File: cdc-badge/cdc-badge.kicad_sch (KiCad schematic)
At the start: 137 parts, among them J1 USB_C, J2 JST S2B-PH-SM4-TB, J3 Conn_02x20_Odd_Even, J4 Conn_Grove, J5 Conn_02x03_Odd_Even, J6 Conn_01x06, J7 Conn_01x24, Q1 Si1308EDL, Q2 SS8050, SW0 0, SW1 1, SW10 YES, SW11 NO, SW12 power on/reset, SW13 reset, SW14 flash/power off, SW15 MST-22D18G2 3J, SW16 MST-22D18G2 3J, SW2 2, SW3 3, SW4 4, SW5 5, SW6 6, SW7 7, SW8 8, SW9 9, U1 ESP32-S3-WROOM-1-N16R8, U2 TCA9535PWR, U3 TROPIC01, U4 TPS613222ADBV, U6 BQ25895RTW, U7 USBLC6-2SC6, U8 TLV62569DBV

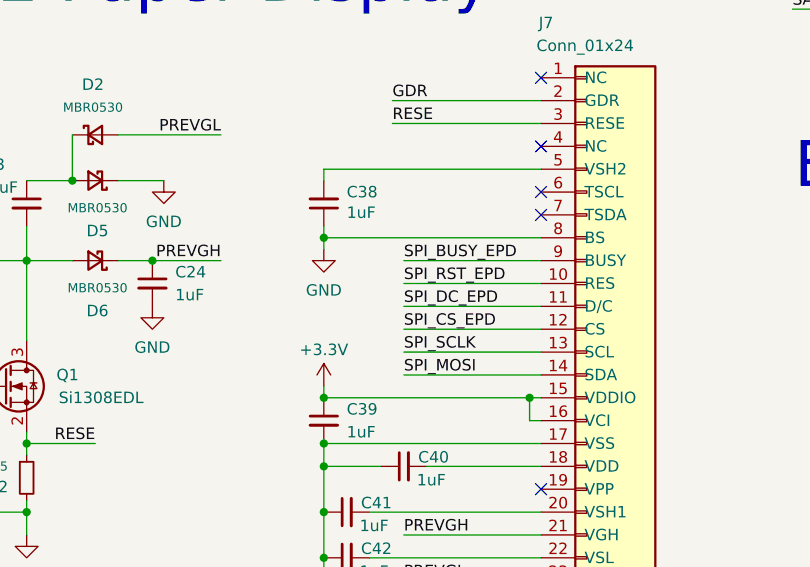
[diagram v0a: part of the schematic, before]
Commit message: schematic: ceetee reviews, e-paper display
Add pull-up on chip select.
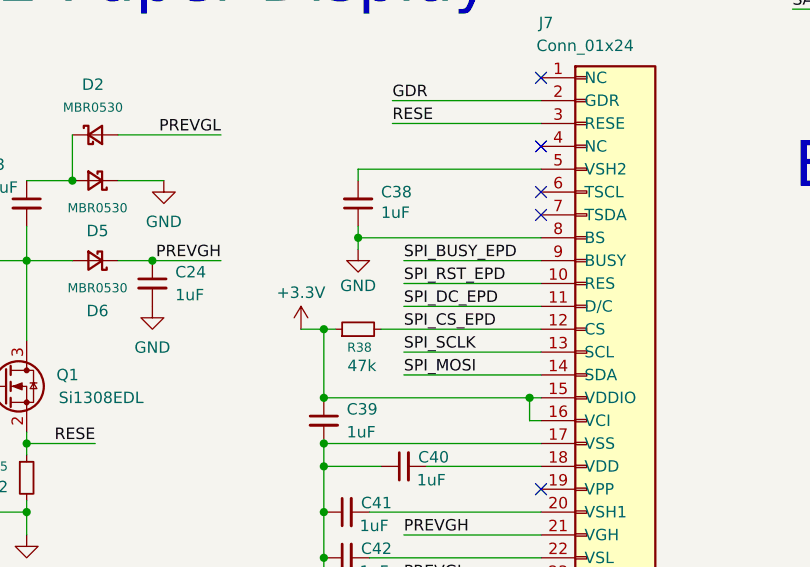
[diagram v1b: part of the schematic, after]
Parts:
- added R38: 47k, Resistor_SMD:R_0603_1608Metric, symbol Device:R_Small
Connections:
- net +3.3V: now also R38.1
- net SPI_CS_EPD: now also R38.2
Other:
- moved on the sheet: C38
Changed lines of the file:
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@@
 	)
 	(junction
+		(at 88.9 246.38)
+		(diameter 0)
+		(color 0 0 0 0)
+	)
+	(junction
 		(at 149.86 76.2)
 		(diameter 0)
@@
 	)
 	(junction
-		(at 88.9 236.22)
+		(at 92.71 236.22)
 		(diameter 0)
 		(color 0 0 0 0)
@@
 	(wire
 		(pts
-			(xy 88.9 229.87) (xy 88.9 228.6)
+			(xy 92.71 229.87) (xy 92.71 228.6)
 		)
 		(stroke
@@
 	(wire
 		(pts
+			(xy 95.25 246.38) (xy 113.03 246.38)
+		)
+		(stroke
+			(width 0)
+			(type default)
+		)
+	)
+	(wire
+		(pts
 			(xy 66.04 238.76) (xy 69.85 238.76)
 		)
@@
 	(wire
 		(pts
+			(xy 86.36 246.38) (xy 88.9 246.38)
+		)
+		(stroke
+			(width 0)
+			(type default)
+		)
+	)
+	(wire
+		(pts
 			(xy 292.1 276.86) (xy 276.86 276.86)
 		)
@@
 	(wire
 		(pts
-			(xy 88.9 237.49) (xy 88.9 236.22)
+			(xy 92.71 237.49) (xy 92.71 236.22)
 		)
 		(stroke
@@
 	(wire
 		(pts
+			(xy 88.9 246.38) (xy 90.17 246.38)
+		)
+		(stroke
+			(width 0)
+			(type default)
+		)
+	)
+	(wire
+		(pts
 			(xy 321.31 60.96) (xy 323.85 60.96)
 		)
@@
 	(wire
 		(pts
-			(xy 88.9 254) (xy 88.9 252.73)
-		)
-		(stroke
-			(width 0)
-			(type default)
-		)
-	)
-	(wire
-		(pts
 			(xy 116.84 50.8) (xy 125.73 50.8)
 		)
@@
 	(wire
 		(pts
-			(xy 88.9 234.95) (xy 88.9 236.22)
+			(xy 92.71 234.95) (xy 92.71 236.22)
 		)
 		(stroke
@@
 	(wire
 		(pts
-			(xy 88.9 254) (xy 111.76 254)
+			(xy 100.33 261.62) (xy 113.03 261.62)
 		)
 		(stroke
@@
 	(wire
 		(pts
-			(xy 100.33 261.62) (xy 113.03 261.62)
+			(xy 44.45 148.59) (xy 52.07 148.59)
 		)
 		(stroke
@@
 	(wire
 		(pts
-			(xy 44.45 148.59) (xy 52.07 148.59)
+			(xy 113.03 180.34) (xy 119.38 180.34)
 		)
 		(stroke
@@
 	(wire
 		(pts
-			(xy 113.03 180.34) (xy 119.38 180.34)
+			(xy 88.9 254) (xy 111.76 254)
 		)
 		(stroke
@@
 	(wire
 		(pts
-			(xy 88.9 228.6) (xy 113.03 228.6)
+			(xy 92.71 228.6) (xy 113.03 228.6)
 		)
 		(stroke
@@
 	(wire
 		(pts
+			(xy 88.9 246.38) (xy 88.9 254)
+		)
+		(stroke
+			(width 0)
+			(type default)
+		)
+	)
+	(wire
+		(pts
 			(xy 149.86 63.5) (xy 162.56 63.5)
 		)
@@
 	(wire
 		(pts
-			(xy 97.79 246.38) (xy 113.03 246.38)
-		)
-		(stroke
-			(width 0)
-			(type default)
-		)
-	)
-	(wire
-		(pts
 			(xy 44.45 157.48) (xy 44.45 153.67)
 		)
@@
 	(wire
 		(pts
-			(xy 88.9 236.22) (xy 113.03 236.22)
+			(xy 92.71 236.22) (xy 113.03 236.22)
 		)
 		(stroke
@@
 	(symbol
 		(lib_id "power:+3.3V")
-		(at 88.9 252.73 0)
+		(at 86.36 246.38 0)
 		(unit 1)
 		(exclude_from_sim no)
@@
 		(dnp no)
 		(property "Reference" "#PWR071"
-			(at 88.9 256.54 0)
+			(at 86.36 250.19 0)
 			(effects
 				(font
@@
 		)
 		(property "Value" "+3.3V"
-			(at 88.9 248.666 0)
+			(at 86.36 242.316 0)
 			(effects
 				(font
@@
 		)
 		(property "Footprint" ""
-			(at 88.9 252.73 0)
+			(at 86.36 246.38 0)
 			(effects
 				(font
@@
 		)
 		(property "Datasheet" ""
-			(at 88.9 252.73 0)
+			(at 86.36 246.38 0)
 			(effects
 				(font
@@
 		)
 		(property "Description" "Power symbol creates a global label with name \"+3.3V\""
-			(at 88.9 252.73 0)
+			(at 86.36 246.38 0)
 			(effects
 				(font
@@
 	(symbol
 		(lib_id "Device:C_Small")
-		(at 88.9 232.41 180)
+		(at 92.71 232.41 180)
 		(unit 1)
 		(exclude_from_sim no)
@@
 		(dnp no)
 		(property "Reference" "C38"
-			(at 91.44 231.14 0)
+			(at 95.25 231.14 0)
 			(effects
 				(font
@@
 		)
 		(property "Value" "1uF"
-			(at 91.44 233.426 0)
+			(at 95.25 233.426 0)
 			(effects
 				(font
@@
 		)
 		(property "Footprint" "Capacitor_SMD:C_0603_1608Metric"
-			(at 88.9 232.41 0)
+			(at 92.71 232.41 0)
 			(effects
 				(font
@@
 		)
 		(property "Datasheet" "~"
-			(at 88.9 232.41 0)
+			(at 92.71 232.41 0)
 			(effects
 				(font
@@
 		)
 		(property "Description" "1uF 50V X5R ±10% 0603 Multilayer Ceramic Capacitor"
-			(at 88.9 232.41 0)
+			(at 92.71 232.41 0)
 			(effects
 				(font
@@
 		)
 		(property "MPN" "CL10A105KB8NNNC"
-			(at 88.9 232.41 0)
+			(at 92.71 232.41 0)
 			(effects
 				(font
@@
 		)
 		(property "JLCPCB PN" "C15849"
-			(at 88.9 232.41 0)
+			(at 92.71 232.41 0)
 			(effects
 				(font
@@
 	(symbol
 		(lib_id "power:GND")
-		(at 88.9 237.49 0)
+		(at 92.71 237.49 0)
 		(unit 1)
 		(exclude_from_sim no)
@@
 		(dnp no)
 		(property "Reference" "#PWR070"
-			(at 88.9 243.84 0)
+			(at 92.71 243.84 0)
 			(effects
 				(font
@@
 		)
 		(property "Value" "GND"
-			(at 88.9 242.062 0)
+			(at 92.71 241.554 0)
 			(effects
 				(font
@@
 		)
 		(property "Footprint" ""
-			(at 88.9 237.49 0)
+			(at 92.71 237.49 0)
 			(effects
 				(font
@@
 		)
 		(property "Datasheet" ""
-			(at 88.9 237.49 0)
+			(at 92.71 237.49 0)
 			(effects
 				(font
@@
 		)
 		(property "Description" "Power symbol creates a global label with name \"GND\" , ground"
-			(at 88.9 237.49 0)
+			(at 92.71 237.49 0)
 			(effects
 				(font
@@
 					(unit 1)
 				)
+			)
+		)
+	)
+	(symbol
+		(lib_id "Device:R_Small")
+		(at 92.71 246.38 90)
+		(unit 1)
+		(exclude_from_sim no)
+		(in_bom yes)
+		(on_board yes)
+		(dnp no)
+		(property "Reference" "R38"
+			(at 94.234 248.412 90)
+			(effects
+				(font
+					(size 1.016 1.016)
+				)
+				(justify left)
+			)
+		)
+		(property "Value" "47k"
+			(at 94.742 250.444 90)
+			(effects
+				(font
+					(size 1.27 1.27)
+				)
+				(justify left)
+			)
+		)
+		(property "Footprint" "Resistor_SMD:R_0603_1608Metric"
+			(at 92.71 246.38 0)
+			(effects
+				(font
+					(size 1.27 1.27)
+				)
+				(hide yes)
+			)
+		)
+		(property "Datasheet" "~"
+			(at 92.71 246.38 0)
+			(effects
+				(font
+					(size 1.27 1.27)
+				)
+				(hide yes)
+			)
+		)
+		(property "Description" "100mW 75V Thick Film Resistor ±1%"
+			(at 92.71 246.38 0)
+			(effects
+				(font
+					(size 1.27 1.27)
+				)
+				(hide yes)
+			)
+		)
+		(property "JLCPCB PN" "C25819"
+			(at 92.71 246.38 0)
+			(effects
+				(font
+					(size 1.27 1.27)
+				)
+				(hide yes)
+			)
+		)
+		(pin "1"
+		)
+		(pin "2"
+		)
+		(instances
+			(project "cdc-badge"
+				(path "/2cec4f7a-7b92-4a21-be0b-2bac184578cb"
+					(reference "R38")
+					(unit 1)
+				)

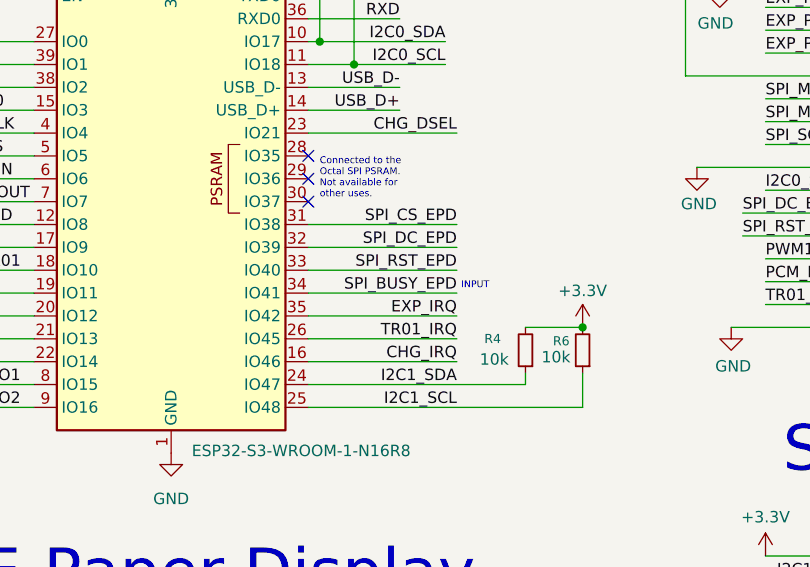
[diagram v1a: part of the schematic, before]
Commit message: schematic: ceetee reviews, fix ESP32 bootstrap pins
IO45 and IO46 must be low during boot. They have internal weak
pull-downs but were connected to nets with strong pull-ups. Now
connecting to nets without any resistors.
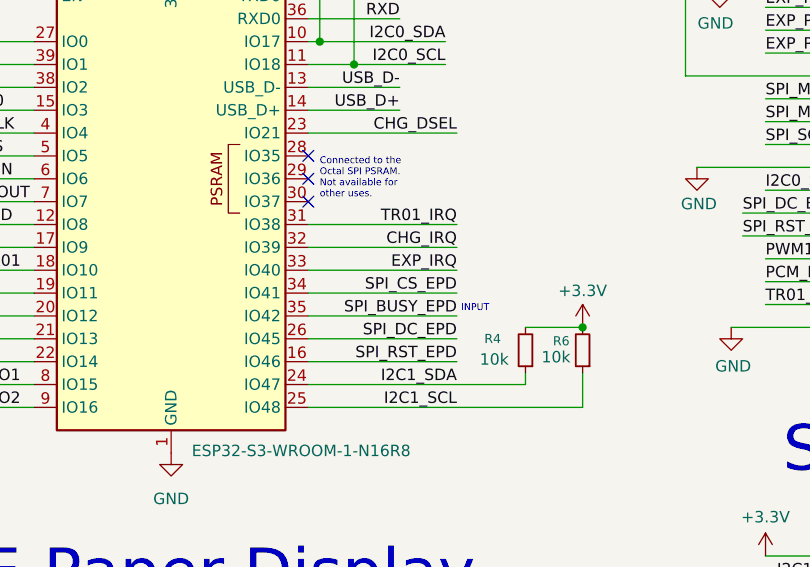
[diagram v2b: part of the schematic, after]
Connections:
- net CHG_IRQ: now also U1.32 (IO39); no longer U1.16 (IO46)
- net EXP_IRQ: now also U1.33 (IO40); no longer U1.35 (IO42)
- net SPI_BUSY_EPD: now also U1.35 (IO42); no longer U1.34 (IO41)
- net SPI_CS_EPD: now also U1.34 (IO41); no longer U1.31 (IO38)
- net SPI_DC_EPD: now also U1.26 (IO45); no longer U1.32 (IO39)
- net SPI_RST_EPD: now also U1.16 (IO46); no longer U1.33 (IO40)
- net TR01_IRQ: now also U1.31 (IO38); no longer U1.26 (IO45)
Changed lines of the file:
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@@
 	(text "INPUT"
 		(exclude_from_sim no)
-		(at 107.442 175.768 0)
+		(at 107.442 178.308 0)
 		(effects
 			(font
@@
 		)
 	)
+	(label "SPI_CS_EPD"
+		(at 105.41 176.53 180)
+		(effects
+			(font
+				(size 1.27 1.27)
+			)
+			(justify right bottom)
+		)
+	)
 	(label "USB_D-"
 		(at 99.06 153.67 180)
@@
 		)
 	)
+	(label "SPI_RST_EPD"
+		(at 105.41 184.15 180)
+		(effects
+			(font
+				(size 1.27 1.27)
+			)
+			(justify right bottom)
+		)
+	)
 	(label "EXP_P14"
 		(at 265.43 144.78 180)
@@
 		)
 	)
-	(label "SPI_CS_EPD"
-		(at 105.41 168.91 180)
-		(effects
-			(font
-				(size 1.27 1.27)
-			)
-			(justify right bottom)
-		)
-	)
 	(label "BTN_YES"
 		(at 287.02 182.88 0)
@@
 		)
 	)
-	(label "SPI_BUSY_EPD"
-		(at 105.41 176.53 180)
-		(effects
-			(font
-				(size 1.27 1.27)
-			)
-			(justify right bottom)
-		)
-	)
 	(label "SPI_CS0"
 		(at 45.72 171.45 0)
@@
 		)
 	)
+	(label "CHG_IRQ"
+		(at 105.41 171.45 180)
+		(effects
+			(font
+				(size 1.27 1.27)
+			)
+			(justify right bottom)
+		)
+	)
 	(label "RESE"
 		(at 63.5 259.08 180)
@@
 		)
 	)
+	(label "EXP_IRQ"
+		(at 105.41 173.99 180)
+		(effects
+			(font
+				(size 1.27 1.27)
+			)
+			(justify right bottom)
+		)
+	)
 	(label "SPI_CS_TR01"
 		(at 248.92 269.24 0)
@@
 		)
 	)
+	(label "SPI_BUSY_EPD"
+		(at 105.41 179.07 180)
+		(effects
+			(font
+				(size 1.27 1.27)
+			)
+			(justify right bottom)
+		)
+	)
 	(label "I2C1_SDA"
 		(at 105.41 186.69 180)
@@
 		)
 	)
-	(label "TR01_IRQ"
-		(at 105.41 181.61 180)
-		(effects
-			(font
-				(size 1.27 1.27)
-			)
-			(justify right bottom)
-		)
-	)
 	(label "SPI_CS1"
 		(at 208.28 163.83 180)
@@
 		)
 	)
-	(label "SPI_RST_EPD"
-		(at 105.41 173.99 180)
-		(effects
-			(font
-				(size 1.27 1.27)
-			)
-			(justify right bottom)
-		)
-	)
 	(label "EPD_LED"
 		(at 144.78 261.62 0)
@@
 		)
 	)
-	(label "BTN_6"
-		(at 265.43 127 180)
+	(label "TR01_IRQ"
+		(at 105.41 168.91 180)
 		(effects
 			(font
@@
 		)
 	)
-	(label "GPCLK0"
-		(at 139.7 139.7 0)
+	(label "BTN_6"
+		(at 265.43 127 180)
 		(effects
 			(font
 				(size 1.27 1.27)
 			)
-			(justify left bottom)
+			(justify right bottom)
 		)
 	)
-	(label "SPI_DC_EPD"
-		(at 105.41 171.45 180)
+	(label "GPCLK0"
+		(at 139.7 139.7 0)
 		(effects
 			(font
 				(size 1.27 1.27)
 			)
-			(justify right bottom)
+			(justify left bottom)
 		)
 	)
@@
 		)
 	)
-	(label "EXP_IRQ"
-		(at 105.41 179.07 180)
+	(label "PREVGL"
+		(at 77.47 224.79 180)
 		(effects
 			(font
@@
 		)
 	)
-	(label "CHG_IRQ"
-		(at 105.41 184.15 180)
+	(label "SPI_SCLK"
+		(at 45.72 179.07 0)
 		(effects
 			(font
 				(size 1.27 1.27)
 			)
-			(justify right bottom)
+			(justify left bottom)
 		)
 	)
-	(label "PREVGL"
-		(at 77.47 224.79 180)
+	(label "SPI_DC_EPD"
+		(at 105.41 181.61 180)
 		(effects
 			(font
@@
 		)
 	)
-	(label "SPI_SCLK"
-		(at 45.72 179.07 0)
-		(effects
-			(font
-				(size 1.27 1.27)
-			)
-			(justify left bottom)
-		)
-	)

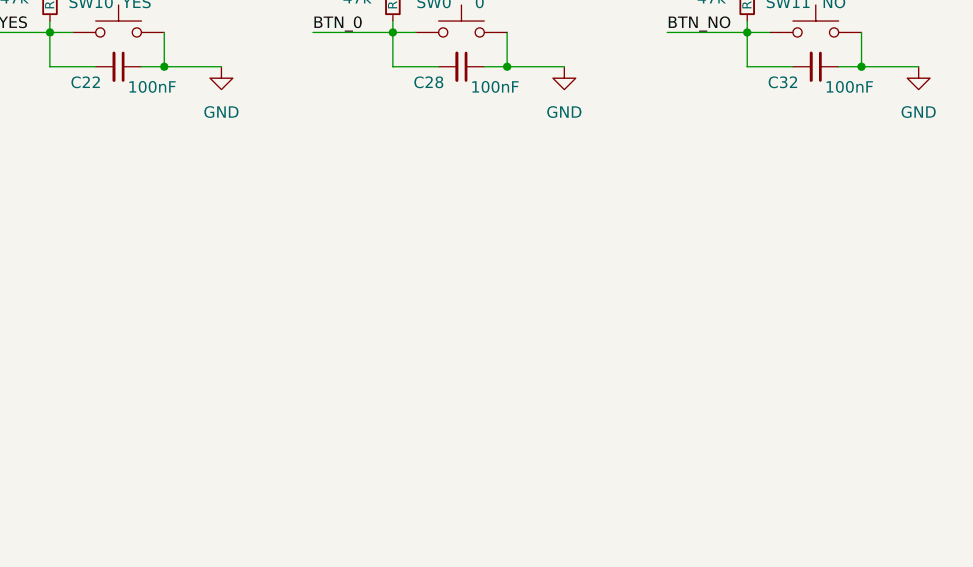
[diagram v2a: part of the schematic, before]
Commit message: Add mounting holes: HAT format and lanyard.
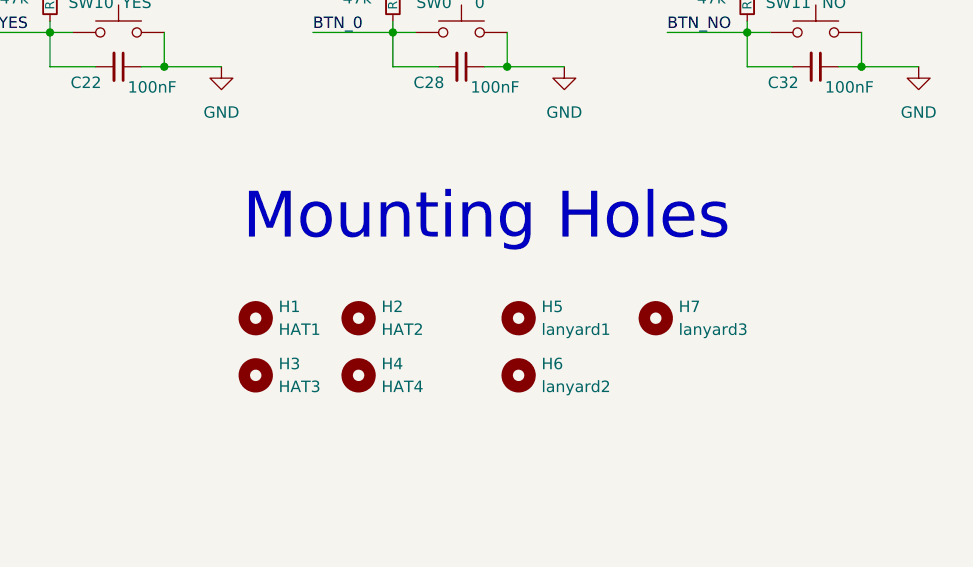
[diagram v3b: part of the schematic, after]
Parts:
- added H1: HAT1, MountingHole:MountingHole_2.7mm, symbol Mechanical:MountingHole
- added H2: HAT2, MountingHole:MountingHole_2.7mm, symbol Mechanical:MountingHole
- added H3: HAT3, MountingHole:MountingHole_2.7mm, symbol Mechanical:MountingHole
- added H4: HAT4, MountingHole:MountingHole_2.7mm, symbol Mechanical:MountingHole
- added H5: lanyard1, MountingHole:MountingHole_5.5mm, symbol Mechanical:MountingHole
- added H6: lanyard2, MountingHole:MountingHole_5.5mm, symbol Mechanical:MountingHole
- added H7: lanyard3, MountingHole:MountingHole_5.5mm, symbol Mechanical:MountingHole
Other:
- note added: "Mounting Holes"

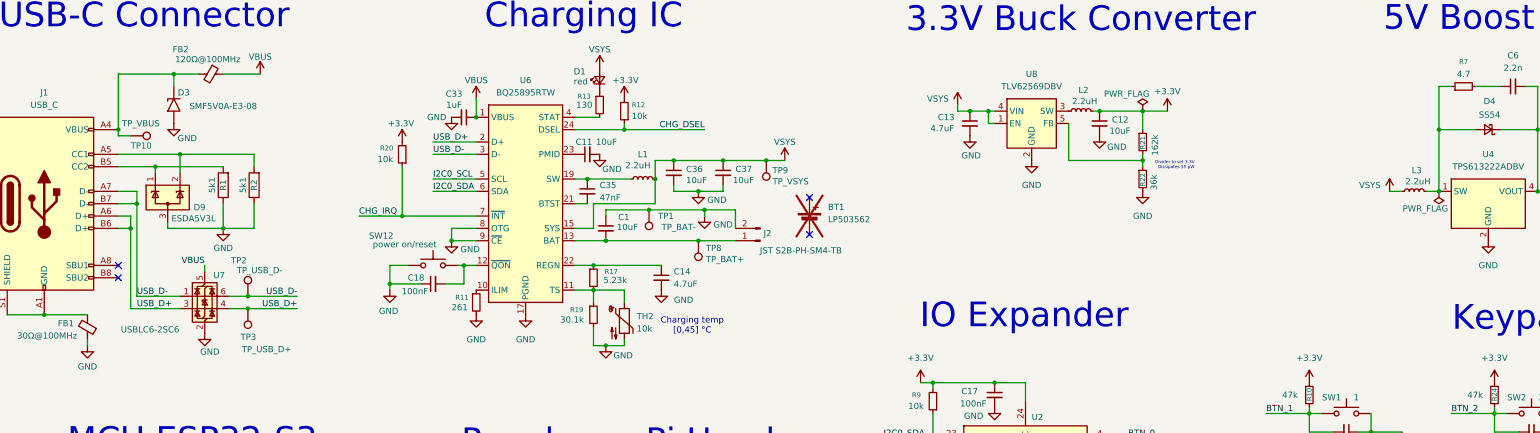
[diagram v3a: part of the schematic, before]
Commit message: schematic: fix ERC errors with exclusions instead of power flags
Power flags just clog the schematic and add no info.
Replaced with exclusions with proper comments.
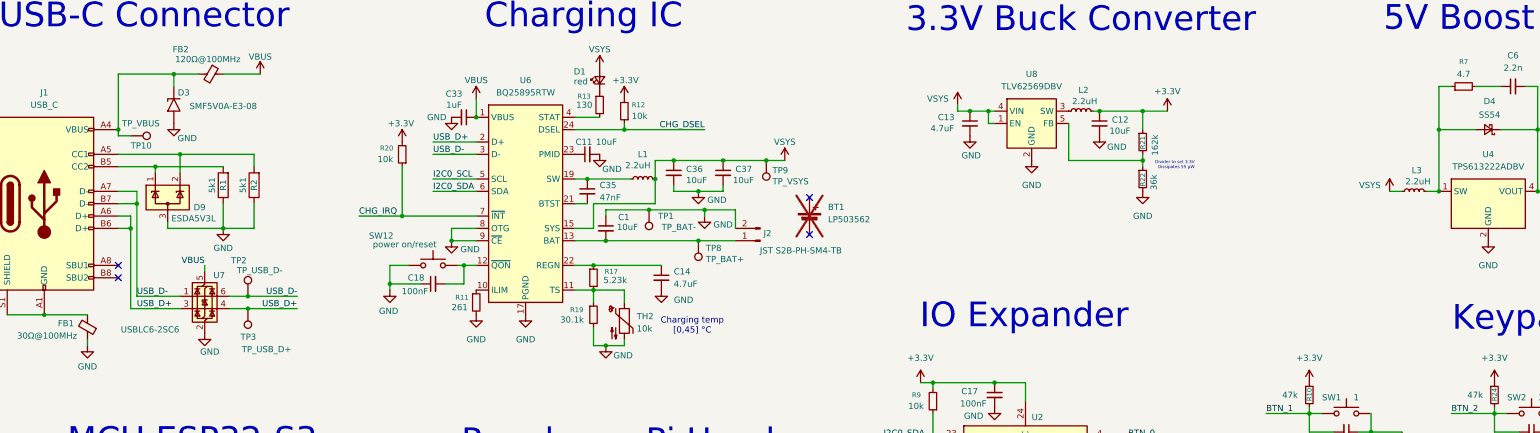
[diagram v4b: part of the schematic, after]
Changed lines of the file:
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@@
 	(wire
 		(pts
-			(xy 45.72 92.71) (xy 45.72 91.44)
+			(xy 45.72 91.44) (xy 45.72 92.71)
 		)
 		(stroke
@@
 	)
 	(symbol
-		(lib_id "power:PWR_FLAG")
-		(at 262.89 44.45 0)
-		(unit 1)
-		(exclude_from_sim no)
-		(in_bom yes)
-		(on_board yes)
-		(dnp no)
-		(property "Reference" "#FLG01"
-			(at 262.89 42.545 0)
-			(effects
-				(font
-					(size 1.27 1.27)
-				)
-				(hide yes)
-			)
-		)
-		(property "Value" "PWR_FLAG"
-			(at 259.588 40.894 0)
-			(effects
-				(font
-					(size 1.27 1.27)
-				)
-			)
-		)
-		(property "Footprint" ""
-			(at 262.89 44.45 0)
-			(effects
-				(font
-					(size 1.27 1.27)
-				)
-				(hide yes)
-			)
-		)
-		(property "Datasheet" "~"
-			(at 262.89 44.45 0)
-			(effects
-				(font
-					(size 1.27 1.27)
-				)
-				(hide yes)
-			)
-		)
-		(property "Description" "Special symbol for telling ERC where power comes from"
-			(at 262.89 44.45 0)
-			(effects
-				(font
-					(size 1.27 1.27)
-				)
-				(hide yes)
-			)
-		)
-		(pin "1"
-		)
-		(instances
-			(project ""
-				(path "/2cec4f7a-7b92-4a21-be0b-2bac184578cb"
-					(reference "#FLG01")
-					(unit 1)
-				)
-			)
-		)
-	)
-	(symbol
 		(lib_id "Mechanical:MountingHole")
 		(at 331.47 214.63 0)
@@
 					(unit 1)
 				)
-			)
-		)
-	)
-	(symbol
-		(lib_id "power:PWR_FLAG")
-		(at 323.85 60.96 180)
-		(unit 1)
-		(exclude_from_sim no)
-		(in_bom yes)
-		(on_board yes)
-		(dnp no)
-		(property "Reference" "#FLG02"
-			(at 323.85 62.865 0)
-			(effects
-				(font
-					(size 1.27 1.27)
-				)
-				(hide yes)
-			)
-		)
-		(property "Value" "PWR_FLAG"
-			(at 321.056 64.516 0)
-			(effects
-				(font
-					(size 1.27 1.27)
-				)
-			)
-		)
-		(property "Footprint" ""
-			(at 323.85 60.96 0)
-			(effects
-				(font
-					(size 1.27 1.27)
-				)
-				(hide yes)
-			)
-		)
-		(property "Datasheet" "~"
-			(at 323.85 60.96 0)
-			(effects
-				(font
-					(size 1.27 1.27)
-				)
-				(hide yes)
-			)
-		)
-		(property "Description" "Special symbol for telling ERC where power comes from"
-			(at 323.85 60.96 0)
-			(effects
-				(font
-					(size 1.27 1.27)
-				)
-				(hide yes)
-			)
-		)
-		(pin "1"
-		)
-		(instances
-			(project "cdc-badge"
-				(path "/2cec4f7a-7b92-4a21-be0b-2bac184578cb"
-					(reference "#FLG02")
-					(unit 1)
-				)
